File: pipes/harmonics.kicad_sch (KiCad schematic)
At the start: 71 parts, among them U10 4046, U11 4046, U12 4046, U13 4017, U14 4017, U15 4017, U16 4046, U17 4046, U18 4017, U19 4017, U4 4046, U5 4046, U6 4046, U7 4017, U8 4017

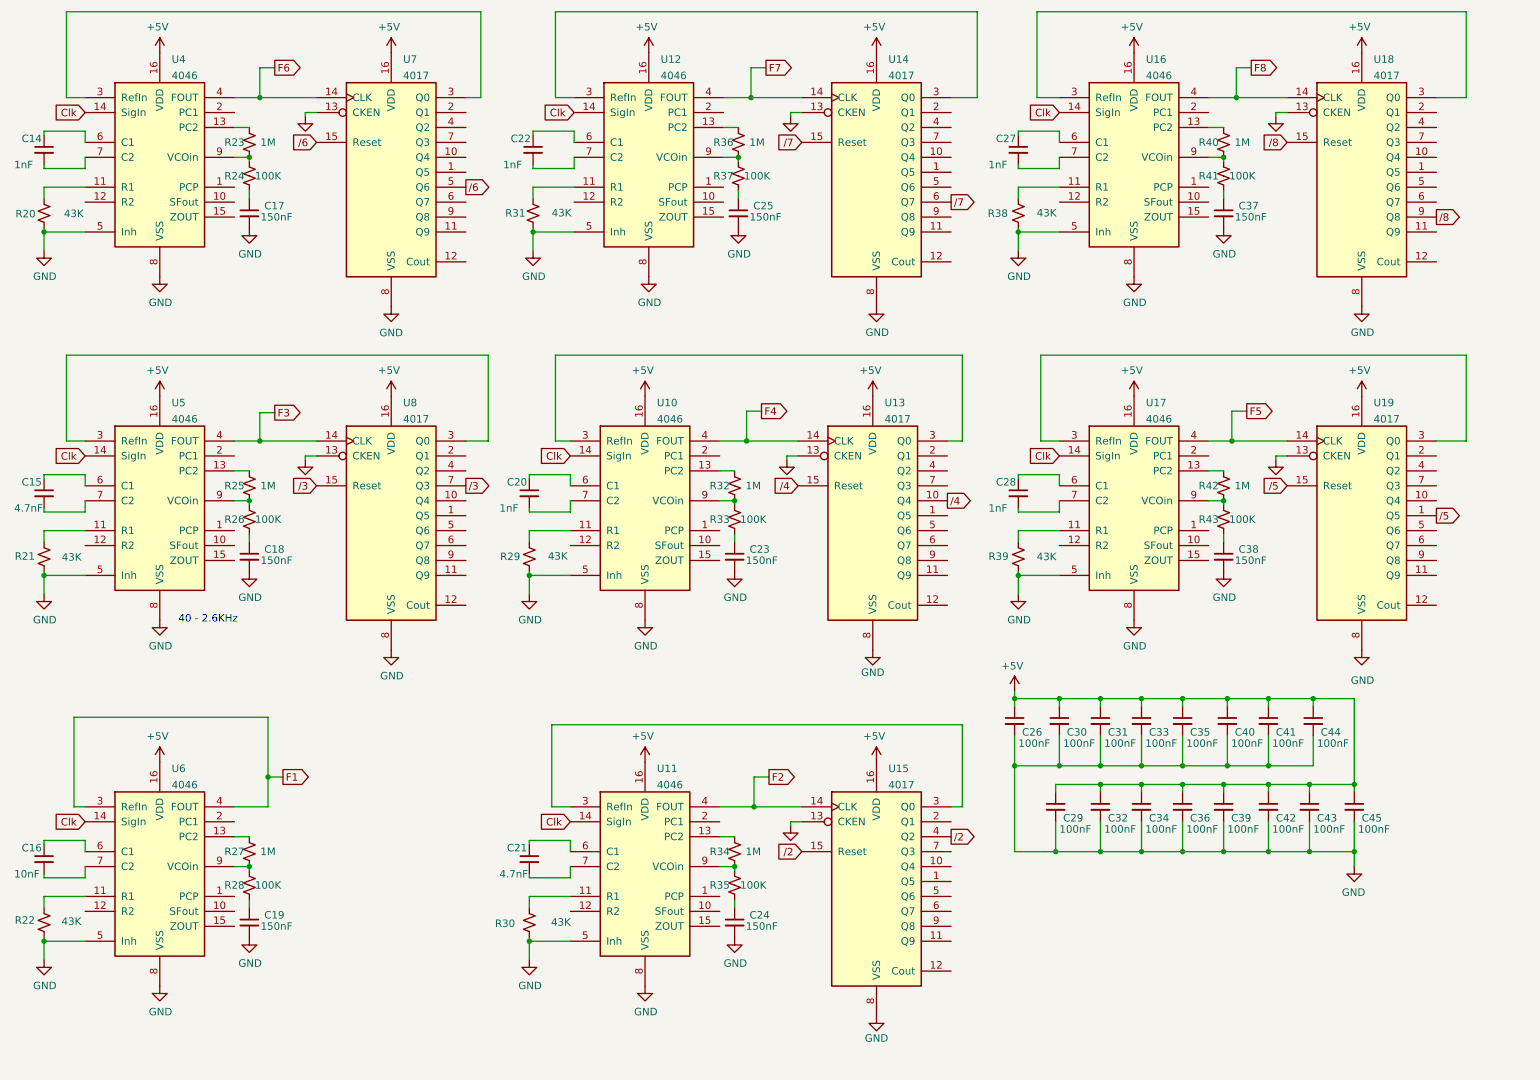
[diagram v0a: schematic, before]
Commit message: Adds harmonic outputs
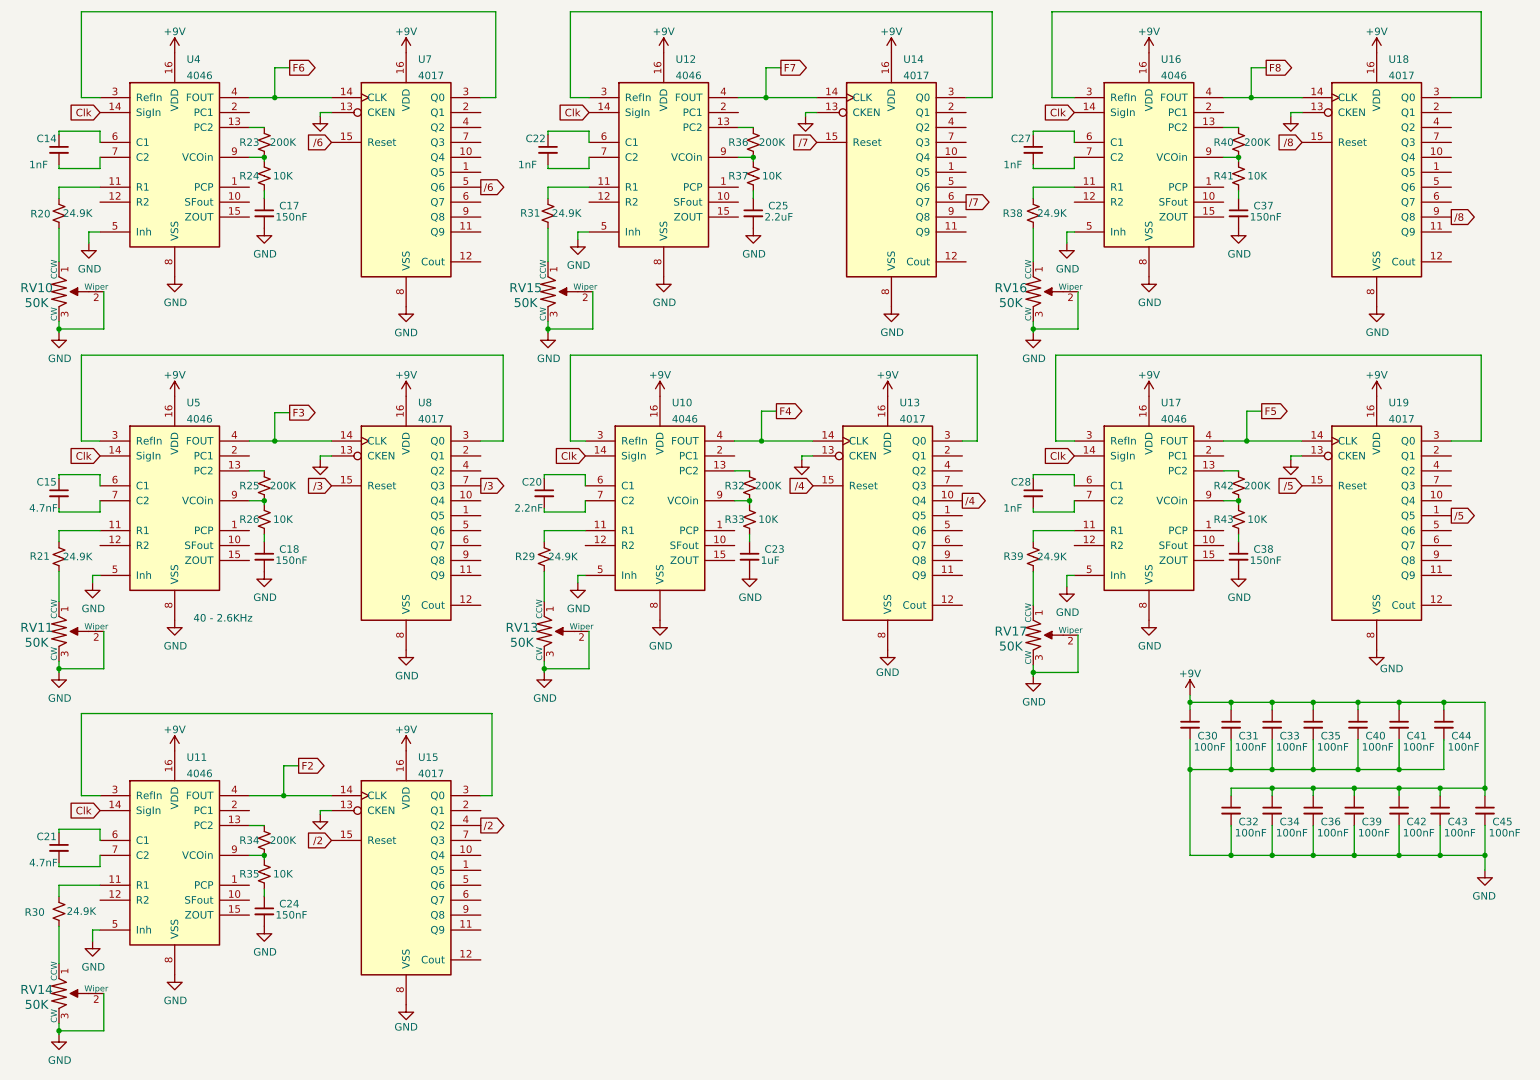
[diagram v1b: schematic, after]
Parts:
- removed C16: 10nF, Capacitor_SMD:C_0805_2012Metric_Pad1.18x1.45mm_HandSolder, symbol Device:C_Small
- removed C19: 150nF, Capacitor_SMD:C_0805_2012Metric_Pad1.18x1.45mm_HandSolder, symbol Device:C_Small
- removed C26, C29: 100nF, Capacitor_SMD:C_0805_2012Metric_Pad1.18x1.45mm_HandSolder, symbol Device:C_Small
- removed R22: 43K, Resistor_SMD:R_0603_1608Metric, symbol Device:R_Small_US
- removed R27: 1M, Resistor_SMD:R_0805_2012Metric_Pad1.20x1.40mm_HandSolder, symbol Device:R_Small_US
- removed R28: 100K, Resistor_SMD:R_0805_2012Metric_Pad1.20x1.40mm_HandSolder, symbol Device:R_Small_US
- removed U6: 4046, Package_SO:TSSOP-16_4.4x5mm_P0.65mm, symbol 4xxx:4046
- added RV10, RV11, RV13, RV14, RV15, RV16, RV17: 50K, sputterizer:Potentiometer_Bourns_3224W_Vertical, symbol dk_Trimmer-Potentiometers:TC33X-2-103E
- C14, C22, C27, C28: LCSC Part # C77484 -> C178423
- C15, C21: LCSC Part # C396761 -> C107104
- C20: value 1nF -> 2.2nF; LCSC Part # C77484 -> C150375
- C23: value 150nF -> 1uF
- C25: value 150nF -> 2.2uF
- R20, R21, R29, R30, R31, R38, R39: value 43K -> 24.9K; LCSC Part # C17695 -> C137761
- R23, R25, R32, R34, R36, R40, R42: value 1M -> 200K; LCSC Part # C17514 -> C104082
- R24, R26, R33, R35, R37, R41, R43: value 100K -> 10K; LCSC Part # C416061 -> C217770
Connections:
- net GND: now also RV10.2 (Wiper), RV10.3 (CW), RV11.2 (Wiper), RV11.3 (CW), RV13.2 (Wiper), RV13.3 (CW), RV14.2 (Wiper), RV14.3 (CW), RV15.2 (Wiper), RV15.3 (CW), RV16.2 (Wiper), RV16.3 (CW), RV17.2 (Wiper), RV17.3 (CW); no longer R20.2, R21.2, R29.2, R30.2, R31.2, R38.2, R39.2
- net +5V renamed +9V
- new net: R31.2, RV15.1 (CCW)
- new net: R39.2, RV17.1 (CCW)
- new net: R38.2, RV16.1 (CCW)
- new net: R21.2, RV11.1 (CCW)
- new net: R30.2, RV14.1 (CCW)
- new net: R20.2, RV10.1 (CCW)
- new net: R29.2, RV13.1 (CCW)
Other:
- moved on the sheet: C14, C15, C17, C18, C20, C21, C22, C23, C24, C25, C27, C28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
